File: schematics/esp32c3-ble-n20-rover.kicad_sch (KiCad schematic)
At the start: 17 parts, among them M1 N20, M2 N20, SW1 SW_SPST, U1 ESP32-C3 SUPERMINI TH, U2 TB6612 (ROB-14450), U3 MT3608 MODULE, U4 TP4056 USB-C

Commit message: fix: optimize decoupling capacitors
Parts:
- removed C1, C4: 680uF, symbol Device:C_Polarized
- C1: renamed from C2; value 680uF -> 100uF
- renumbered C3 to C2, C5 to C3, C6 to C4
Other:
- moved on the sheet: C2

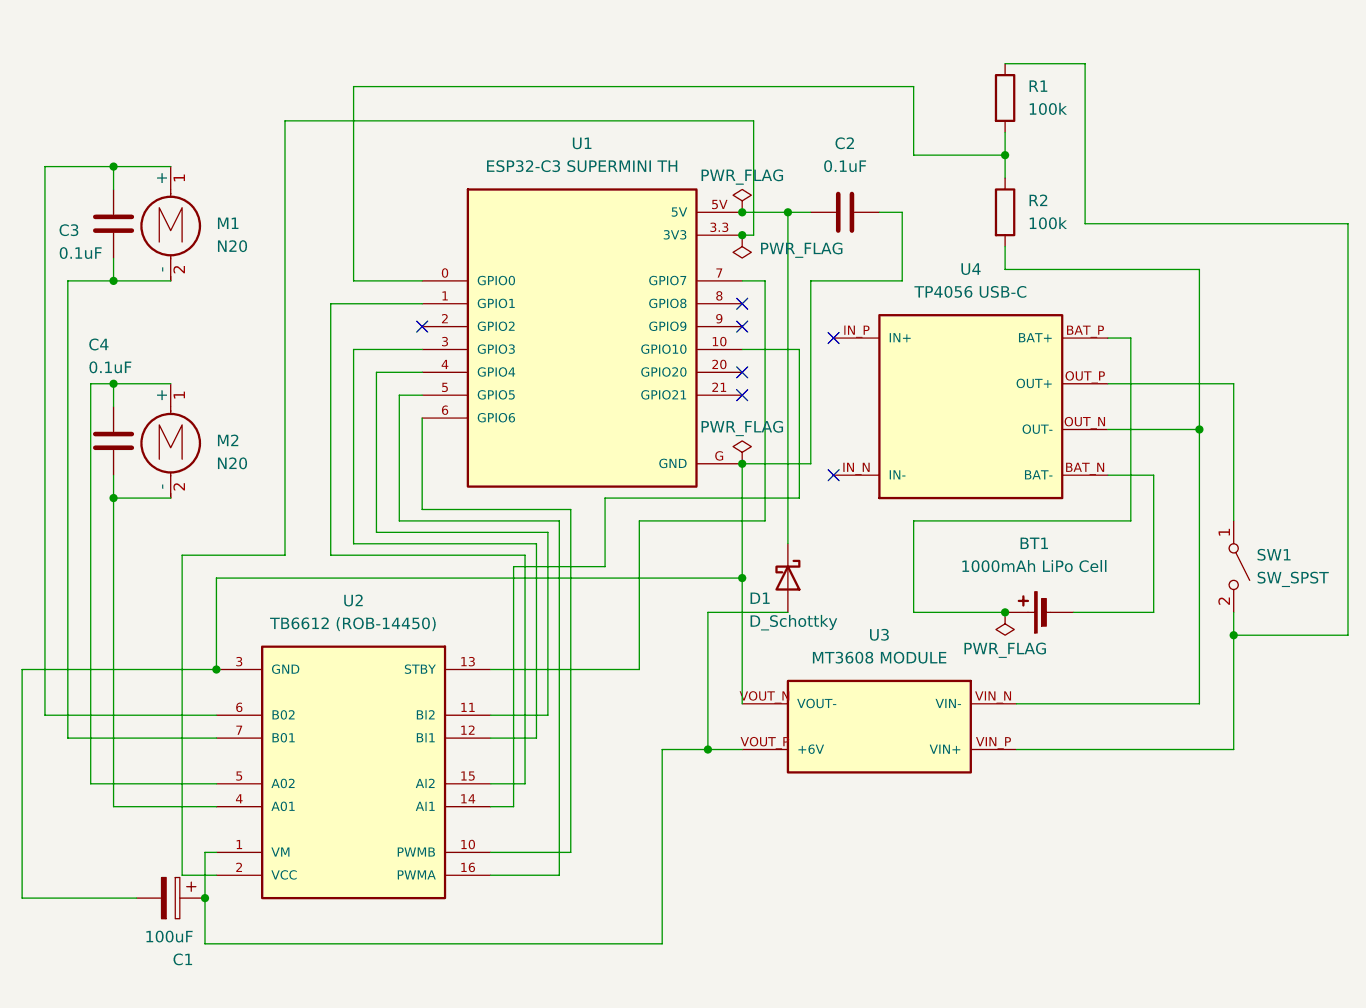
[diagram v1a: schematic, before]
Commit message: feat: add current-sense shunt on boost convertor ground return
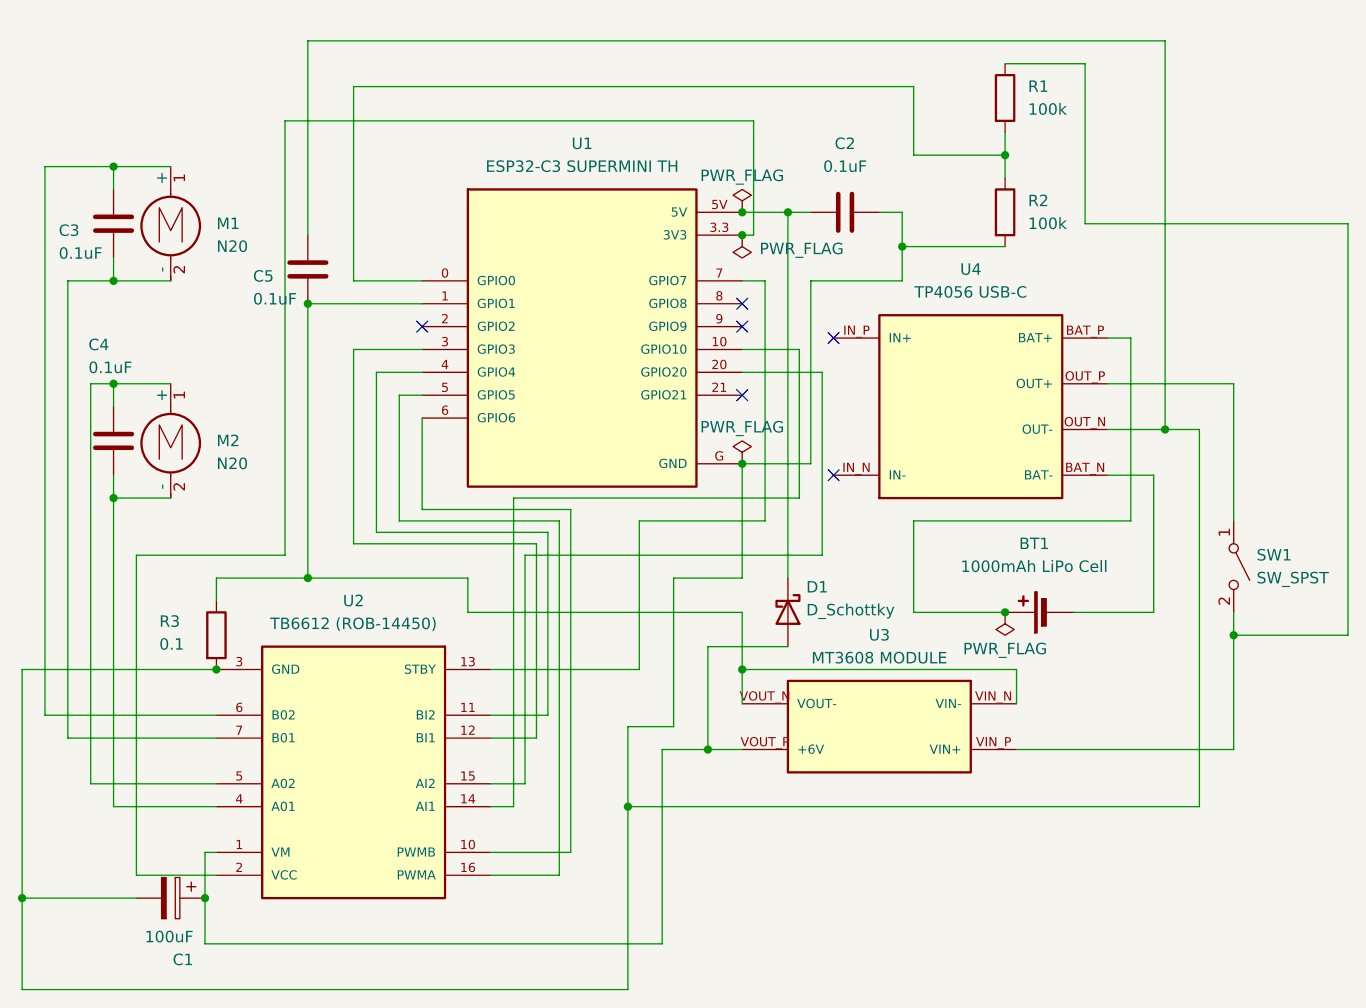
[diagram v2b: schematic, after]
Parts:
- added C5: 0.1uF, symbol Device:C
- added R3: 0.1, symbol Device:R
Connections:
- net GND: now also R2.2, U4.OUT_N (OUT-), C5.1, R3.2; no longer U3.VOUT_N (VOUT-)
- net at U2.15 (AI2): now also U1.20 (GPIO20); no longer U1.1 (GPIO1)
- new net: C5.2, R3.1, U1.1 (GPIO1), U3.VIN_N (VIN-), U3.VOUT_N (VOUT-)
- no-connect marks 7 -> 6
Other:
- moved on the sheet: D1
